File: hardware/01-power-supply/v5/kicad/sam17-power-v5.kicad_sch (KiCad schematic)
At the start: 157 parts, among them J1 KPJX-PM-4S, J10 PinHeader 1x04 P2.54mm, J2 Molex KK-254 4 pos (con llave), J5 Faston 6.3x0.8 PCB, J6 Molex KK-254 2 pos, J8 PinHeader 1x04 P2.54mm, J9 Molex KK-254 2 pos, Q2 N-MOSFET 60V 40A Ron<5mohm, SW1 Pulsador tactil 6x6mm THT, U1 Linear Tech LT1963AEST#TRPBF, U10 TI ADS1115IDGSR, U11 TI TMP1075DGKR, U12 TI INA226AIDGSR, U13 TI INA226AIDGSR, U14 TI INA226AIDGSR, U15 TI LM74502DDFR, U16 TI TPS26630PWPR, U17 TI MSP430FR2111IPW16, U18 TI TPS70933DBVR, U19 TI TPS26630PWPR, U2 Linear Tech LT3015EQ#TRPBF, U20 TI LM393BDR, U21 TI TL431BIDBZR, U22 TI TL431BIDBZR, U23 TI TL431BIDBZR, U24 TI TL431BIDBZR, U25 TI TL431BIDBZR, U4 Linear Tech LT3045EDD#TRPBF, U5 Linear Tech LT3045EDD#TRPBF, U6 Linear Tech LT3094EDD#PBF, U7 Linear Tech LT3094EDD#PBF, U8 TI INA226AIDGSR, U9 TI ISO1541D

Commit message: hardware: fuente v5, rehace el esquematico contra las hojas de datos
El esquematico anterior no habria funcionado aunque la placa estuviera
ruteada. Lo verificado contra las hojas del repo:

- Simbolos propios con el pinout inventado: TPS26630 (SHDN e IN_SYS a
  masa, IN/OUT/PowerPAD al aire), LM74502 (GND en +24 V, GATE en GND),
  MSP430 (DVCC/DVSS en dos GPIO), TRACO THN y Mornsun URB con las
  salidas cambiadas, LT3015 con el TAB (= IN) a GND, LT1963A en un
  SOT-223 que solo existe en version fija, Q2 sin ningun pad.
- Cableado: PGFB de los LT3045/LT3094 a GND y VIOC a GND, R_SET de
  120k con dos reguladores en paralelo (24 V en vez de 12 V), INA226
  U13/U14 en 0x48/0x49 chocando con ADS1115/TMP1075, BAT54S pegando las
  entradas del ADC a 0.3 V, TL431 de los crowbar cortocircuitando la
  puerta en vez de dispararla, VCAP del LM74502 al aire, EN del TPS709
  (7 V max) en +24 V, U19 colgando de un detector que mira su propia
  salida, PS3 no aislado sin camino de retorno a GND24.
- Valores: el filtro LC de la BOM no era el que analizan los
  presupuestos (con el de la BOM, U1 ve 21 V > 20 V), divisores de
  OVP/UVLO y trims de TRACO que no daban las tensiones documentadas.
- BOM: ~45 de 55 codigos LCSC eran de otra pieza.

Ahora:
- build_simbolos.py y build_huellas.py generan los simbolos y huellas
  propios desde tablas con su pagina de hoja; donde KiCad trae el
  simbolo correcto (TPS26631PWP, LT1963AEQ, LT3015Q, TL431DBZ...) se usa
  el suyo. TPS26630PWPR no existe: va el TPS26631PWPR.
- build_schematic.py escribe la hoja sin MCP (symlib + schcheck, como
  VCO y bus board), exige declarar cada patilla y cruza patillas con
  pads; ERC 0 infracciones con todas las severidades. UUID
  deterministas.
- Decisiones: GND24-GNDA unidas solo en NT1 (PS3), el LC sigue al
  analisis (22 uH / 47 uF / 0.68 ohm + 220 uF), crowbar TL431 -> PNP ->
  SCR, D-F4 referido a VREF con histeresis, D1 bidireccional, conector
  de panel fuera de la PCB (bom-chasis.csv), dos salidas 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
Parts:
- removed C3, C4: 22uF 25V X7R 1210, Capacitor_SMD:C_1210_3225Metric, symbol Device:C
- removed D10: Bourns SMBJ16A TVS, Diode_SMD:D_SMB, symbol Device:D_TVS
- removed J1: KPJX-PM-4S, sam17:Kycon_KPJX-PM-4S, symbol sam17:KPJX-PM-4S
- removed PS1: TRACO THN 30-2422WI, sam17:Converter_DCDC_TRACO_THN-30WI_THT, symbol sam17:TRACO_THN_30-2422WI
- removed PS2: Mornsun URB2405YMD-20WR3, sam17:Converter_DCDC_Mornsun_URB-YMD-20WR3_THT, symbol sam17:Mornsun_URB2405YMD-20WR3
- removed PS3: Mornsun K7805T-1000R3, sam17:Converter_DCDC_Mornsun_K78_T1000R3_SMD, symbol sam17:Mornsun_K7805T-1000R3
- removed PS4, PS5: TRACO THN 20-2413WI, sam17:Converter_DCDC_TRACO_THN-20WI_THT, symbol sam17:TRACO_THN_20-2413WI
- removed Q2: N-MOSFET 60V 40A Ron<5mohm, Package_TO_SOT_SMD:TDSON-8-1, symbol Device:Q_NMOS
- removed R19, R29, R30: 20 mohm 1% 1W 2512, Resistor_SMD:R_2512_6332Metric, symbol Device:R_Shunt
- removed R20: 100 mohm 1% 1W 2512, Resistor_SMD:R_2512_6332Metric, symbol Device:R_Shunt
- removed U1: Linear Tech LT1963AEST#TRPBF, Package_TO_SOT_SMD:SOT-223-3_TabPin2, symbol sam17:LT1963AEST
- removed U15: TI LM74502DDFR, Package_TO_SOT_SMD:SOT-23-8, symbol sam17:LM74502DDFR
- removed U16, U19: TI TPS26630PWPR, Package_SO:HTSSOP-20-1EP_4.4x6.5mm_P0.65mm_EP3.4x6.5mm, symbol sam17:TPS26630PWPR
- removed U18: TI TPS70933DBVR, Package_TO_SOT_SMD:SOT-23-5, symbol Regulator_Linear:LP2985-3.3
- removed U2: Linear Tech LT3015EQ#TRPBF, Package_TO_SOT_SMD:TO-263-5_TabPin3, symbol sam17:LT3015EQ
- removed U20: TI LM393BDR, Package_SO:SOIC-8_3.9x4.9mm_P1.27mm, symbol sam17:LM393BDR
- removed U21, U22, U23, U24, U25: TI TL431BIDBZR, Package_TO_SOT_SMD:SOT-23, symbol Reference_Voltage:TL431LP
- added C10, C30, C31, C32, C33, C34, C35, C9: 100nF 50V X7R, Capacitor_SMD:C_0805_2012Metric, symbol Device:C
- added C11, C13: 22nF 50V X7R, Capacitor_SMD:C_0805_2012Metric, symbol Device:C
- added C12: 1nF 50V C0G, Capacitor_SMD:C_0805_2012Metric, symbol Device:C
- added C14: 100uF 50V, Capacitor_SMD:CP_Elec_8x10, symbol Device:C_Polarized
- added C15: 10uF 50V X7R, Capacitor_SMD:C_1210_3225Metric, symbol Device:C
- added C16, C36, C37, C38: 22uF 25V X7R, Capacitor_SMD:C_1210_3225Metric, symbol Device:C
- added C29: 100uF 25V, Capacitor_SMD:CP_Elec_6.3x7.7, symbol Device:C_Polarized
- added C3, C4: 47uF 35V, Capacitor_SMD:CP_Elec_6.3x7.7, symbol Device:C_Polarized
- added D10: SMBJ16A, Diode_SMD:D_SMB, symbol Device:D_Zener
- added D2: BZT52C30, Diode_SMD:D_SOD-123, symbol Device:D_Zener
- added J1: Bornera 2P 5.0 mm, TerminalBlock:TerminalBlock_MaiXu_MX126-5.0-02P_1x02_P5.00mm, symbol Connector:Conn_01x02_Pin
- added J3: Bornera 4P 5.08 mm, TerminalBlock_Phoenix:TerminalBlock_Phoenix_MKDS-1,5-4-5.08_1x04_P5.08mm_Horizontal, symbol Connector:Conn_01x04_Pin
- added J7: Molex KK-254 4P, Connector_Molex:Molex_KK-254_AE-6410-04A_1x04_P2.54mm_Vertical, symbol Connector:Conn_01x04_Pin
- added NT1: NetTie GND24-GNDA, NetTie:NetTie-2_SMD_Pad2.0mm, symbol Device:NetTie_2
- added PS1: THN 30-2422WI, Converter_DCDC:Converter_DCDC_TRACO_THL30-xxxxWI_THT, symbol sam17:TRACO_THN_Dual
- added PS2: URB2405YMD-20WR3, sam17:Converter_DCDC_Mornsun_URB_YMD-20WR3_Horizontal_THT, symbol sam17:Mornsun_URB_YMD-20WR3
- added PS3: K7805T-1000R3, sam17:Converter_DCDC_Mornsun_K78_T-1000R3_SMD, symbol sam17:Mornsun_K78xxT-1000R3
- added PS4, PS5: THN 20-2413WI, Converter_DCDC:Converter_DCDC_TRACO_THL30-xxxxWI_THT, symbol sam17:TRACO_THN_Single
- added Q2: CSD18534Q5A, Package_TO_SOT_SMD:TDSON-8-1, symbol Transistor_FET:CSD18534Q5A
- added Q3, Q4, Q5, Q6: MMBT3906, Package_TO_SOT_SMD:SOT-23, symbol Transistor_BJT:MMBT3906
- added R19, R29, R30: 0.02, Resistor_SMD:R_2512_6332Metric, symbol Device:R
- added R20: 0.1, Resistor_SMD:R_2512_6332Metric, symbol Device:R
- added R61, R62: 120k 0.1%, Resistor_SMD:R_0805_2012Metric, symbol Device:R
- added R63: 1.2k, Resistor_SMD:R_0805_2012Metric, symbol Device:R
- added R64: 220, Resistor_SMD:R_0805_2012Metric, symbol Device:R
- added R65: 47k, Resistor_SMD:R_0805_2012Metric, symbol Device:R
- added R66, R68, R74, R75, R76, R77: 10k, Resistor_SMD:R_0805_2012Metric, symbol Device:R
- added R67: 6.8M, Resistor_SMD:R_0805_2012Metric, symbol Device:R
- added R69: 10M, Resistor_SMD:R_0805_2012Metric, symbol Device:R
- added R70, R71, R72, R73: 1k, Resistor_SMD:R_0805_2012Metric, symbol Device:R
- added R78, R79, R80, R81: 100, Resistor_SMD:R_0805_2012Metric, symbol Device:R
- added U1: LT1963AEQ, Package_TO_SOT_SMD:TO-263-5_TabPin3, symbol Regulator_Linear:LT1963AEQ
- added U15: LM74502DDFR, Package_TO_SOT_SMD:SOT-23-8, symbol sam17:LM74502DDF
- added U16, U19: TPS26631PWPR, Package_SO:HTSSOP-20-1EP_4.4x6.5mm_P0.65mm_EP3.4x6.5mm_Mask2.96x2.96mm_ThermalVias, symbol Power_Management:TPS26631PWP
- added U18: TPS70933DBVR, Package_TO_SOT_SMD:SOT-23-5, symbol sam17:TPS70933DBV
- added U2: LT3015EQ, Package_TO_SOT_SMD:TO-263-5_TabPin3, symbol Regulator_Linear:LT3015Q
- added U20: LM393B, Package_SO:SOIC-8_3.9x4.9mm_P1.27mm, symbol Comparator:LM393
- added U21, U22, U23, U24, U25: TL431BI, Package_TO_SOT_SMD:SOT-23, symbol Reference_Voltage:TL431DBZ
- C1, C2: value 47uF 25V electrolitico SMD -> 220uF 35V; footprint Capacitor_SMD:CP_Elec_6.3x7.7 -> Capacitor_SMD:CP_Elec_8x10; LCSC (none) -> C178562; MPN (none) -> EEEFK1V221P
- C17, C18: value 10uF 25V X7R 1206 -> 47uF 35V; footprint Capacitor_SMD:C_1206_3216Metric -> Capacitor_SMD:CP_Elec_6.3x7.7; LCSC (none) -> C249923; MPN (none) -> VZH470M1VTR-0607
- C19, C21: value 470nF 25V X7R 0805 -> 470nF 50V X7R; LCSC (none) -> C13967; MPN (none) -> CL21B474KBFNNNE
- C20, C22: value 10uF 25V X7R 1206 -> 22uF 25V X7R; footprint Capacitor_SMD:C_1206_3216Metric -> Capacitor_SMD:C_1210_3225Metric; LCSC (none) -> C21397; MPN (none) -> GRM32ER71E226KE15L
- C23, C24, C25, C26, C27, C28, C5, C6: value 100nF 50V X7R 0805 -> 100nF 50V X7R; LCSC (none) -> C49678; MPN (none) -> CC0805KRX7R9BB104
- C7: value 1uF 50V X7R 0805 -> 1uF 50V X7R; LCSC (none) -> C28323; MPN (none) -> CL21B105KBFNNNE
- C8: value 1uF 50V X7R 0805 -> 4.7uF 25V X7R; LCSC (none) -> C354262; MPN (none) -> CC0805KKX7R8BB475
- D1: value Bourns SMBJ26A TVS -> SMBJ26CA; LCSC (none) -> C83332; MPN (none) -> SMBJ26CA
- D11: value Schottky BAT54WS 30V 200mA -> BAT54WS; LCSC (none) -> C124205; MPN (none) -> BAT54WS-7-F
- D12, D13: value 1N4001 / S1M -> S1M; LCSC (none) -> C144860; MPN (none) -> S1M-E3/61T
- D14, D15, D16, D17: value Diodo Schottky doble BAT54S -> BAT54S; LCSC (none) -> C19726; MPN (none) -> BAT54SLT1G
- D18: value LED azul 0805 -> LED verde 0805; LCSC (none) -> C98221; MPN (none) -> LTST-C170KGKT
- D3: LCSC (none) -> C99771; MPN (none) -> 204-10SURD/S530-A3-L
- D4: LCSC (none) -> C85160; MPN (none) -> 204-10UYD/S530-A3-L
- D6: LCSC (none) -> C181864; MPN (none) -> 204-10SYGD/S530-E2-L
- D7: LCSC (none) -> C86881; MPN (none) -> 204-10SUBC/S400-A4
- F2, F3: value Bourns SF-1206F300-2 3.0A Fast Blow -> SF-1206F300-2 3A; LCSC (none) -> C208499; MPN (none) -> SF-1206F300-2
- F4: value Bourns SF-1206F200-2 2.0A Fast Blow -> SF-1206F200-2 2A; LCSC (none) -> C719183; MPN (none) -> SF-1206F200-2
- F5: value Bourns SF-1206F400-2 4.0A Fast Blow -> 0466004 4A; LCSC (none) -> C187596; MPN (none) -> 0466004.NRHF
- FB1, FB2: value Ferrita 60 ohm @ 100MHz 2A -> BLM21PG600SN1D; footprint Resistor_SMD:R_0805_2012Metric -> Inductor_SMD:L_0805_2012Metric; LCSC (none) -> C18305; MPN (none) -> BLM21PG600SN1D
- J10, J8: value PinHeader 1x04 P2.54mm -> PinHeader 1x04; LCSC (none) -> C2691448; MPN (none) -> PZ254V-11-04P
- J2: value Molex KK-254 4 pos (con llave) -> Molex KK-254 4P; LCSC (none) -> C504991; MPN (none) -> 22-27-2041
- J5: MPN (none) -> 3866A.68
- J6, J9: value Molex KK-254 2 pos -> Molex KK-254 2P; LCSC (none) -> C293316; MPN (none) -> 22-27-2021
- L2, L3: value 10uH 2.5A DCR<35mohm -> 22uH SRR1260-220M; LCSC (none) -> C3224283; MPN (none) -> SRR1260-220M
- R1, R2: value 2.2k 1/4W 0805 -> 2.2k; LCSC (none) -> C17520; MPN (none) -> 0805W8F2201T5E
- R10, R9: value 120k 0.1% 25ppm 0805 -> 120k 0.1%; LCSC (none) -> C865161; MPN (none) -> RT0805BRD07120KL
- R11: value 4.02k 1% 0805 -> 4.02k; LCSC (none) -> C17663; MPN (none) -> 0805W8F4021T5E
- R12, R35: value 49.9k 0.1% 0805 -> 49.9k 0.1%; LCSC (none) -> C469661; MPN (none) -> RT0805BRD0749K9L
- R13: value 3.32k 0.1% 0805 -> 1.62k 0.1%; LCSC (none) -> C50670348; MPN (none) -> TC0525B1621T5G
- R14: value 2.00k 0.1% 0805 -> 1.96k 0.1%; LCSC (none) -> C2093012; MPN (none) -> TNPW08051K96BEEN
- R15, R16, R17, R18: value 20 mohm 1% 1W 2512 -> 0.02; LCSC (none) -> C553969; MPN (none) -> WSL2512R0200FEA
- R21, R22, R23, R24: value 100k 0.1% 0805 -> 100k 0.1%; LCSC (none) -> C122537; MPN (none) -> RT0805BRD07100KL
- R25, R26, R27, R28: value 20.0k 0.1% 0805 -> 20.0k 0.1%; LCSC (none) -> C469660; MPN (none) -> RT0805BRD0720KL
- R3, R4: value 680R 1/4W 0805 -> 680; LCSC (none) -> C17798; MPN (none) -> 0805W8F6800T5E
- R31: value 1.0k 1% 0805 -> 220; LCSC (none) -> C17557; MPN (none) -> 0805W8F2200T5E
- R32, R33: value 240k 1% 0805 -> 45.3k; LCSC (none) -> C17701; MPN (none) -> 0805W8F4532T5E
- R34: value 18.2k 1% 0805 -> 18.2k; LCSC (none) -> C17497; MPN (none) -> 0805W8F1822T5E
- R36: value 3.83k 0.1% 0805 -> 3.9k 0.1%; LCSC (none) -> C865471; MPN (none) -> RT0805BRD073K9L
- R37, R38: value 0.5 ohm 1% 1206 -> 0.68; LCSC (none) -> C19108; MPN (none) -> 1206W4F680LT5E
- R39: value 49.9k 0.1% 0805 -> 47.5k 0.1%; LCSC (none) -> C865514; MPN (none) -> RT0805BRD0747K5L
- R40, R47, R48, R50, R52: value 10.0k 0.1% 0805 -> 10.0k 0.1%; LCSC (none) -> C110775; MPN (none) -> RT0805BRD0710KL
- R41: value 49.9k 0.1% 0805 -> 10.2k 0.1%; LCSC (none) -> C865134; MPN (none) -> RT0805BRD0710K2L
- R42: value 10.0k 0.1% 0805 -> 59.0k 0.1%; LCSC (none) -> C865570; MPN (none) -> RT0805BRD0759KL
- R43: value 100k 1% 0805 -> 100k; LCSC (none) -> C149504; MPN (none) -> 0805W8F1003T5E
- R44: value 10.0k 1% 0805 -> 10k; LCSC (none) -> C17414; MPN (none) -> 0805W8F1002T5E
- R45, R46: value 45.3k 0.1% 0805 -> 45.3k 0.1%; LCSC (none) -> C866072; MPN (none) -> RT0805BRE0745K3L
- R49: value 13.3k 0.1% 0805 -> 13.3k 0.1%; LCSC (none) -> C865182; MPN (none) -> RT0805BRD0713K3L
- R5: value 8.66k 0.1% 0805 -> 9.31k 0.1%; LCSC (none) -> C865720; MPN (none) -> RT0805BRD079K31L
- R51: value 12.7k 0.1% 0805 -> 12.7k 0.1%; LCSC (none) -> C50670219; MPN (none) -> TC0525B1272T5G
- R53, R54, R55, R56: value 1.0k 1% 0805 -> 1k; LCSC (none) -> C17513; MPN (none) -> 0805W8F1001T5E
- R57, R58, R59, R60: value 2.2k 1% 0805 -> 2.2k; LCSC (none) -> C17520; MPN (none) -> 0805W8F2201T5E
- R6, R8: value 1.00k 0.1% 0805 -> 1.00k 0.1%; LCSC (none) -> C110774; MPN (none) -> RT0805BRD071KL
- R7: value 9.09k 0.1% 0805 -> 9.09k 0.1%; LCSC (none) -> C865717; MPN (none) -> RT0805BRD079K09L
- RV2, RV3: value Bourns 3296W-1-102 (1k trimmer) -> 1k 3296W; LCSC (none) -> C57089; MPN (none) -> 3296W-1-102LF
- SCR1, SCR2, SCR3, SCR4: value NXP BT151-500R Tiristor TO-220 -> BT151-500R; LCSC (none) -> C9211; MPN (none) -> BT151-500R,127
- SW1: value Pulsador tactil 6x6mm THT -> Pulsador 6x6; LCSC (none) -> C93157; MPN (none) -> B3F-1000
- TP1, TP10, TP11, TP2, TP3, TP4, TP5, TP6, TP7, TP8, TP9: value TestPoint Pad D2.0mm -> TestPoint; MPN (none) -> —
- U10: value TI ADS1115IDGSR -> ADS1115IDGS; footprint Package_SO:MSOP-10_3x3mm_P0.5mm -> Package_SO:TSSOP-10_3x3mm_P0.5mm; LCSC (none) -> C37593; MPN (none) -> ADS1115IDGSR
- U11: value TI TMP1075DGKR -> TMP1075DGK; LCSC (none) -> C2864807; MPN (none) -> TMP1075DGKR
- U12, U13, U14, U8: value TI INA226AIDGSR -> INA226; footprint Package_SO:MSOP-10_3x3mm_P0.5mm -> Package_SO:TSSOP-10_3x3mm_P0.5mm; LCSC (none) -> C49851; MPN (none) -> INA226AIDGSR
- U17: value TI MSP430FR2111IPW16 -> MSP430FR2111IPW16; LCSC (none) -> C2052845; MPN (none) -> MSP430FR2111IPW16R
- U4, U5: value Linear Tech LT3045EDD#TRPBF -> LT3045EDD; footprint Package_DFN_QFN:DFN-10-1EP_3x3mm_P0.5mm_EP1.65x2.38mm -> Package_DFN_QFN:DFN-10-1EP_3x3mm_P0.5mm_EP1.65x2.38mm_ThermalVias; LCSC (none) -> C514420; MPN (none) -> LT3045EDD#TRPBF
- U6, U7: value Linear Tech LT3094EDD#PBF -> LT3094EDD; footprint Package_DFN_QFN:DFN-12-1EP_3x3mm_P0.45mm_EP1.65x2.38mm -> Package_DFN_QFN:DFN-12-1EP_3x3mm_P0.45mm_EP1.65x2.38mm_ThermalVias; LCSC (none) -> C670493; MPN (none) -> LT3094EDD#TRPBF
- U9: value TI ISO1541D -> ISO1541; LCSC (none) -> C143028; MPN (none) -> ISO1541DR
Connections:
- net +12V_FUSED_RACK: now also R29.1; no longer R45.1, SCR1.2 (A), U13.8 (Vbus), U13.9 (Vin-)
- net +12V_RAW_RACK: now also PS1.3 (+Vout)
- net +12V_ULTRA: now also J7.4 (Pin_4), R19.2
- net +13V1: now also U4.6 (PGFB), U5.6 (PGFB), C36.1, U1.4 (OUT)
- net +15V5_EFUSE: now also U19.18 (OUT), U19.19 (OUT), U19.20 (OUT)
- net +15V5_FILT: now also D10.1 (K), U1.2 (IN)
- net +15V5_LC: now also C3.1; no longer C24.1, C25.1, C26.1, C27.1, D14.2 (K), D15.2 (K), D16.2 (K), D17.2 (K), F4.1, R25.2, R27.2, R28.2, R41.1, R44.1, R57.1, R58.1, U10.8 (VDD), U11.7 (A0), U11.8 (V+), U12.10 (Vin+), U12.2 (A0), U12.6 (VS), U12.8 (Vbus), U12.9 (Vin-), U13.6 (VS), U14.2 (A0), U14.6 (VS), U8.6 (VS), U9.1 (VCC1)
- net +15V5_RAW: now also PS4.3 (+Vout), U19.1 (IN), U19.2 (IN), U19.3 (IN), U19.6 (IN_SYS); no longer R32.2
- net +24V_PROT: now also Q2.5 (D), R64.1, U16.1 (IN), U16.2 (IN), U16.3 (IN), U16.6 (IN_SYS); no longer C7.1
- net +24V_RAW: now also C10.1, C9.2, J1.1 (Pin_1), Q2.1 (S), Q2.2 (S), Q2.3 (S), U15.1 (EN/UVLO), U15.5 (VS), U15.8 (SRC)
- net +24V_SW: now also C14.1, C15.1, PS1.1 (+Vin), PS2.3 (Vin), PS3.1 (+Vin), PS3.2 (+Vin), PS4.1 (+Vin), PS5.1 (+Vin), U16.18 (OUT), U16.19 (OUT), U16.20 (OUT)
- net +3V3_MCU: now also U17.5 (DVCC), R65.1, R66.1, U18.5 (OUT); no longer U17.13 (VDD)
- net +5V_DIG: now also Q6.2 (E), R77.1
- net +5V_FUSED_RACK: now also R30.1; no longer J6.1 (Pin_1), R3.1, R49.1, SCR3.2 (A), TP5.1, U14.8 (Vbus), U14.9 (Vin-)
- net +5V_RAW_DIG: now also C29.1, PS2.4 (+Vo)
- net -12V9: now also U6.5 (PGFB), U7.5 (PGFB), C37.2, U2.5 (OUT)
- net -12V_RACK: now also J3.3 (Pin_3), U23.3 (A)
- net -12V_RAW_RACK: now also PS1.5 (-Vout)
- net -12V_ULTRA: now also J7.1 (Pin_1)
- net -15V5_FILT: now also U2.3 (IN)
- net -15V5_LC: now also C4.2
- net -15V5_RAW: now also PS5.5 (-Vout)
- net ADJ_U1: now also U1.5 (ADJ)
- net ADJ_U2: now also U2.4 (ADJ)
- net AIN0: now also D14.3 (COM); no longer D14.1 (A)
- net AIN1: now also D15.3 (COM); no longer D15.1 (A)
- net AIN2: now also D16.3 (COM); no longer D16.1 (A)
- net AIN3: now also D17.3 (COM); no longer D17.1 (A)
- net FLT_M5: now also U17.1 (P1.1), R66.2, U16.15 (~{FLT}); no longer U17.2 (P1.1_FLT)
- net GATE_Q2: now also Q2.4 (G), U15.6 (GATE)
- net GATE_SCR1: now also R78.2
- net GATE_SCR2: now also R79.2
- net GATE_SCR3: now also R80.2
- net GATE_SCR4: now also R81.2
- net GND24: now also U17.6 (DVSS), C10.2, C11.2, C12.2, C14.2, C15.2, C16.2, D2.2 (A), J1.2 (Pin_2), NT1.1, PS1.2 (-Vin), PS2.2 (GND), PS3.3 (GND), PS3.7 (GND), PS4.2 (-Vin), PS5.2 (-Vin), U15.2 (GND), U15.7 (OV), U16.16 (PGTH), U16.21 (GND), U16.9 (GND), U18.2 (GND); no longer U17.14 (VSS)
- net GNDA: now also D14.1 (A), D15.1 (A), D16.1 (A), D17.1 (A), R32.2, C13.2, C3.2, C30.2, C31.2, C32.2, C33.2, C34.2, C35.2, C36.2, C37.1, C38.2, C4.1, D10.2 (A), J3.2 (Pin_2), J7.2 (Pin_2), J7.3 (Pin_3), NT1.2, PS1.4 (Common), PS4.5 (-Vout), PS5.3 (+Vout), Q4.2 (E), R61.2, R62.2, R68.2, R75.1, U1.3 (GND), U19.12 (MODE), U19.16 (PGTH), U19.21 (GND), U19.7 (UVLO), U19.9 (GND), U2.2 (GND), U20.4 (V-), U21.3 (A), U22.3 (A), U24.3 (A); no longer D14.3 (COM), D15.3 (COM), D16.3 (COM), D17.3 (COM), U4.6 (PGFB), U5.6 (PGFB), U6.5 (PGFB), U6.7 (VIOC), U7.5 (PGFB), U7.7 (VIOC)
- net GNDD: now also C29.2, PS2.6 (0V), U25.3 (A)
- net ILIM_U16: now also U16.11 (ILIM)
- net ILIM_U19: now also U19.11 (ILIM)
- net LED_CTRL: now also U17.14 (P1.4); no longer U17.5 (P1.4_LED)
- net MCU_RST: now also U17.4 (RST/NMI/SBWTDIO), C12.1, R65.2; no longer U17.11 (RST)
- net MCU_TEST: now also U17.3 (TEST/SBWTCK); no longer U17.12 (TEST)
- net OUTS_POS: now also C38.1, R19.1
- net REF_CB1: now also U22.2 (REF)
- net REF_CB2: now also U23.2 (REF)
- net REF_CB3: now also U24.2 (REF)
- net REF_CB4: now also U25.2 (REF)
- net SDA_A: no longer U13.1 (A1), U14.1 (A1)
- net SENSE_NEG: now also C35.1, U20.6 (-)
- net SENSE_POS: now also C34.1, R67.2, U20.3 (+)
- net SET_NEG: now also R62.1
- net SET_POS: now also R61.1
- net SHDN_CASCADE: now also R67.1, R69.1, U1.1 (~{SHDN}), U2.1 (~{SHDN}), U20.1, U20.7
- net SHDN_M5: now also U17.15 (P1.3), U16.13 (~{SHDN}); no longer U17.4 (P1.3_SHDN)
- net SW_RESET: now also U17.13 (P1.5); no longer U17.6 (P1.5_RSTBTN)
- net TRIM_PS4: now also PS4.4 (Trim)
- net TRIM_PS5: now also PS5.4 (Trim)
- net UVLO_U16: now also U16.7 (UVLO)
- net VREF_2V5: now also R41.1, R63.2, U20.2 (-), U21.1 (K), U21.2 (REF)
- net OVPR_U16 renamed OVP_U16
- net OVP_U16: now also U16.8 (OVP)
- net OVPR_U19 renamed OVP_U19
- net OVP_U19: now also U19.8 (OVP)
- new net +12V_RACK: J3.1 (Pin_1), Q3.2 (E), R29.2, R45.1, R74.1, SCR1.2 (A), U13.8 (Vbus), U13.9 (Vin-)
- new net +24V_LDO: C7.1, D2.1 (K), R64.2, U18.1 (IN)
- new net +5V_AUX: C24.1, C25.1, C26.1, C27.1, C30.1, C31.1, C32.1, C33.1, D14.2 (K), D15.2 (K), D16.2 (K), D17.2 (K), J6.1 (Pin_1), R20.2, R25.2, R27.2, R28.2, R44.1, R57.1, R58.1, R63.1, U10.8 (VDD), U11.7 (A0), U11.8 (V+), U12.2 (A0), U12.6 (VS), U12.8 (Vbus), U12.9 (Vin-), U13.1 (A1), U13.6 (VS), U14.1 (A1), U14.2 (A0), U14.6 (VS), U20.8 (V+), U8.6 (VS), U9.1 (VCC1)
- new net +5V_RACK: J3.4 (Pin_4), Q5.2 (E), R3.1, R30.2, R49.1, R76.1, SCR3.2 (A), TP5.1, U14.8 (Vbus), U14.9 (Vin-)
- new net +5V_RAW_RACK: C16.1, F4.1, PS3.4 (+Vout), PS3.5 (+Vout), R20.1, U12.10 (Vin+)
- new net DVDT_U16: C11.1, U16.10 (dVdT)
- new net DVDT_U19: C13.1, U19.10 (dVdT)
- new net QB_CB1: Q3.1 (B), R70.1, R74.2
- new net QB_CB2: Q4.1 (B), R71.1, R75.2
- new net QB_CB3: Q5.1 (B), R72.1, R76.2
- new net QB_CB4: Q6.1 (B), R73.1, R77.2
- new net QC_CB1: Q3.3 (C), R78.1
- new net QC_CB2: Q4.3 (C), R79.1
- new net QC_CB3: Q5.3 (C), R80.1
- new net QC_CB4: Q6.3 (C), R81.1
- new net REF0_NEG: R68.1, R69.2, U20.5 (+)
- new net TLK_CB1: R70.2, U22.1 (K)
- new net TLK_CB2: R71.2, U23.1 (K)
- new net TLK_CB3: R72.2, U24.1 (K)
- new net TLK_CB4: R73.2, U25.1 (K)
- new net VCAP_U15: C9.1, U15.4 (VCAP)
- no-connect marks 0 -> 41
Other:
- note added: "BLOQUE CON: Conectores"
- note added: "BLOQUE DCDC: Convertidores: THN 30 (+-12 rack), URB (+5 digital M1), K78 (+5 rack), 2 x THN 20 (+-15.5)"
- note added: "BLOQUE DF4: Detector D-F4: LM393 + TL431, umbral 14.5 V con histeresis"
- note added: "BLOQUE DF6: Rack: fusibles y crowbars D-F6 (TL431 -> PNP -> BT151)"
- note added: "BLOQUE LC: Tope M3 (#334): TPS26631 + filtro LC 22 uH / 47 uF / 0.68 ohm + 220 uF + SMBJ16A"
- note added: "BLOQUE M5: Entrada 24 V, polaridad (LM74502 + CSD18534Q5A), eFuse U16 y supervisor M5"
- note added: "BLOQUE PRE: Pre-reguladores LT1963A (+13.1 V) y LT3015 (-12.9 V)"
- note added: "BLOQUE TEL: Telemetria I2C: 4 x INA226, ADS1115, TMP1075 e ISO1541"
- note added: "BLOQUE ULTRA: Cascada ultra: 2 x LT3045 y 2 x LT3094 en paralelo, R_SET = 60k"
- note added: "PWR_FLAG: redes que alimenta algo pasivo o un conector"
- note removed: "BLOQUE 1: Entrada 24V, Supervisor M5 (MSP430FR2111 + TPS26630) y Proteccion Inversa (LM74502)"
- note removed: "BLOQUE 2: DC-DCs (TRACO THN 30WI +-12V, Mornsun URB 5V DIG, Mornsun K78 5V RACK, 2x THN 20WI +-15.5V)"
- note removed: "BLOQUE 3: Filtro LC y eFuse TPS26630 M3 / #334 + Bourns SMBJ16A"
- note removed: "BLOQUE 4: Secuenciador D-F4 / M4 (LM393B + TL431BI)"
- note removed: "BLOQUE 5: Cascada Primera Etapa (LT1963A + LT3015)"
- note removed: "BLOQUE 6: Cascada Segunda Etapa Ultra-Bajo Ruido (2x LT3045 + 2x LT3094)"
- note removed: "BLOQUE 7: Protecciones Rack Crowbar D-F6 (4x BT151-500R + TL431BI + Fuses)"
- note removed: "BLOQUE 8: Telemetria I2C Aislada (4x INA226, ADS1115, TMP1075, ISO1541)"
- note removed: "SAM17 FUENTE v5 (LADRILLO EXTERNO 24V + 5 CONVERTIDORES DC-DC)"
- company: SAM17 — Sintetizador analogico modular -> SAM17 - Sintetizador analogico modular
- title: SAM17 Modulo 01 v5 — Fuente de Alimentacion Ladrillo 24V y DC-DCs -> SAM17 Modulo 01 v5 - Fuente: ladrillo 24 V y convertidores DC-DC

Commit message: hardware: fuente v5, SHDN de U16 con pull-down, FLT de U19 al MSP430 y U19 con rueda libre
- U16: R83 (47k) de SHDN a GND24. El pin tiene pull-up interno (2,48 a
  3,3 V en vacio, hasta 10 uA, tps2663.pdf p. 7): sin pull-down, U16
  encendia en cada enchufe, reset o sesion de programacion antes de que
  el MCU leyera la bandera de abandono de la FRAM.
- U19: FLT a P1.2 del MSP430, con pull-up R84. No va al SHDN de U16: el
  TPS26631 baja FLT mientras su entrada esta en UVLO (p. 19) y U16 no
  arrancaria nunca.
- U19: UVLO a IN_SYS por R82 (6,8M, p. 20). A GND elegia el umbral
  interno de 15,1 a 15,9 V (p. 6), por encima del riel de 15,5 V.
- D19 (SS34) de OUT de U19 a GNDA: al abrir U19 la corriente de L2 no
  tenia camino y llevaba OUT por debajo de sus -0,3 V (p. 5, 36 y 38).
- U18: R64 pasa a 1k y D2 a BZT52C24. Con el BZT52C30 el TPS709 llegaba a
  32 V con 2 mA; ahora no pasa de 26,4 V con D1 en 42,1 V.
- R53 a R56 (R_GK) pasan a 100 ohm: el dV/dt de 200 V/us del BT151 se da
  con R_GK = 100 ohm (nxp-bt151-500r.pdf p. 6).

check_netlist comprueba cada uno; con la netlist anterior salen los nueve
en rojo.
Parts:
- added D19: SS34, Diode_SMD:D_SMA, symbol Device:D_Schottky
- added R82: 6.8M, Resistor_SMD:R_0805_2012Metric, symbol Device:R
- added R83: 47k, Resistor_SMD:R_0805_2012Metric, symbol Device:R
- added R84: 10k, Resistor_SMD:R_0805_2012Metric, symbol Device:R
- D2: value BZT52C30 -> BZT52C24; LCSC C163721 -> C171749; MPN BZT52C30-7-F -> BZT52C24-7-F
- R53, R54, R55, R56: value 1k -> 100; LCSC C17513 -> C17408; MPN 0805W8F1001T5E -> 0805W8F1000T5E
- R64: value 220 -> 1k; LCSC C17557 -> C17513; MPN 0805W8F2200T5E -> 0805W8F1001T5E
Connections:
- net +15V5_EFUSE: now also D19.1 (K)
- net +15V5_RAW: now also R82.1
- net +3V3_MCU: now also R84.1
- net GND24: now also R83.2
- net GNDA: now also D19.2 (A); no longer U19.7 (UVLO)
- net SHDN_M5: now also R83.1
- net FLT_U19: now reaches U19.15 (~{FLT})
- net FLT_U19: now also U17.16 (P1.2), R84.2
- new net UVLO_U19: R82.2, U19.7 (UVLO)
- no-connect marks 41 -> 39
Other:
- moved on the sheet: C1, C11, C12, C13, C14, C15, C16, C17, C18, C19, C2, C20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

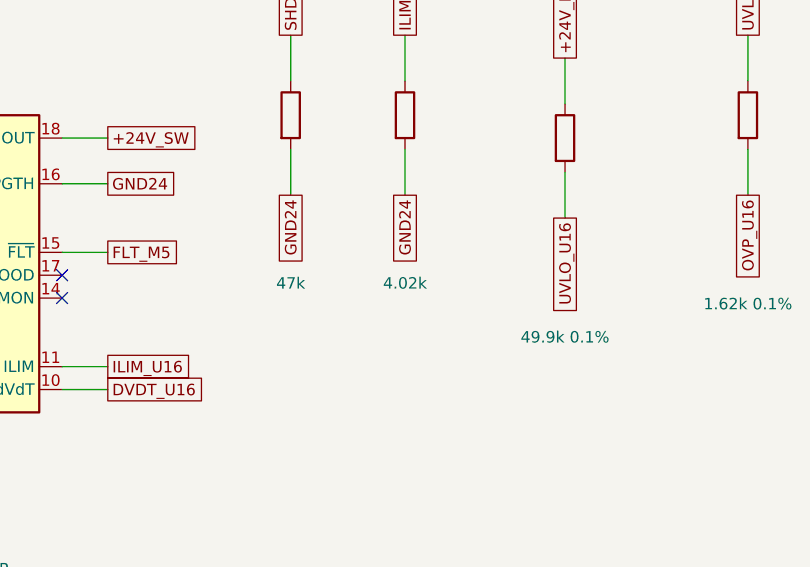
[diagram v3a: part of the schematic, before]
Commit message: hardware: fuente v5, placa y fabricacion con R11 de 3,74 kOhm
build_pcb.py --desde-ruteo copia ahora tambien el valor de cada huella
desde el netlist, asi que un cambio de valor no pide otro Freerouting. La
placa sale del ruteo guardado de la corrida anterior:

- El cobre es el mismo salvo una conexion del rescate en +24V_RAW hasta
  U15.1, que pasa de 5 tramos a 2 (1506 pistas, 285 vias).
- DRC (kicad-cli 10.0.3, todas las severidades, zonas rellenas y paridad
  con el esquematico): 0 infracciones, 0 sin conectar, 0 de paridad.

lcsc_snapshot.csv entra C2960937 y sale C17663. Esquematico, netlist, fab/
y pcb/ regenerados.
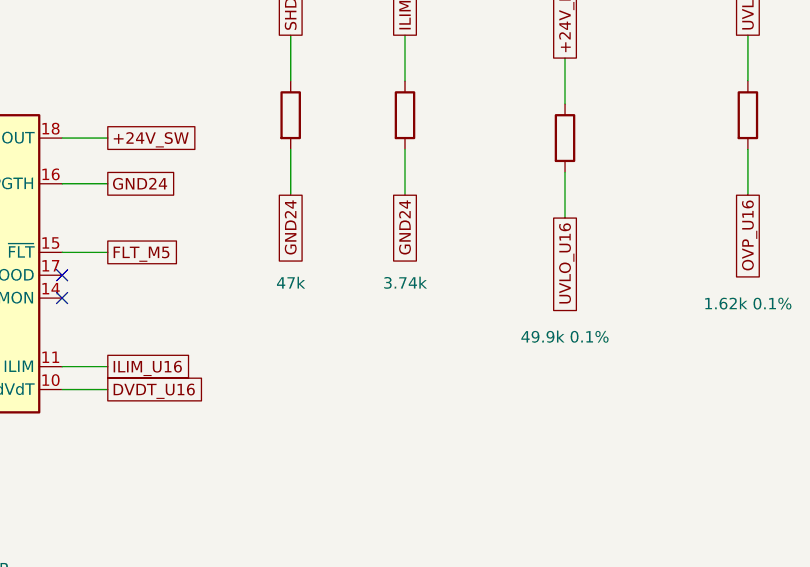
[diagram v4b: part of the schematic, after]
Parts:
- R11: value 4.02k -> 3.74k; LCSC C17663 -> C2960937; MPN 0805W8F4021T5E -> FRC0805F3741TS
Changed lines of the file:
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@@
 			)
 		)
-		(property "Value" "4.02k"
+		(property "Value" "3.74k"
 			(at 106.68 132.98 0)
 			(show_name no)
@@
 			)
 		)
-		(property "LCSC" "C17663"
+		(property "LCSC" "C2960937"
 			(at 106.68 114.3 0)
 			(hide yes)
@@
 			)
 		)
-		(property "MPN" "0805W8F4021T5E"
+		(property "MPN" "FRC0805F3741TS"
 			(at 106.68 114.3 0)
 			(hide yes)

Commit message: hardware: fuente v5, placa y fabricacion con R11 de vuelta en 4,02 kOhm
Desde el ruteo guardado, con build_pcb.py --desde-ruteo: el cobre es el de
la placa anterior, tramo a tramo (1506 pistas, 285 vias). DRC (kicad-cli
10.0.3, todas las severidades, zonas rellenas y paridad con el
esquematico): 0 infracciones, 0 sin conectar, 0 de paridad.

lcsc_snapshot.csv vuelve a C17663 y sale C2960937.
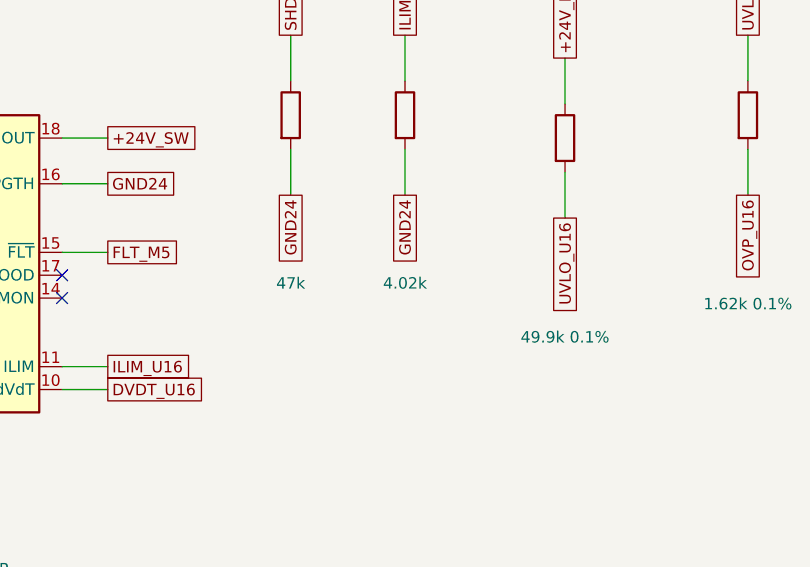
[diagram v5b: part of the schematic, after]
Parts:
- R11: value 3.74k -> 4.02k; LCSC C2960937 -> C17663; MPN FRC0805F3741TS -> 0805W8F4021T5E
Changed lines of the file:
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@@
 			)
 		)
-		(property "Value" "3.74k"
+		(property "Value" "4.02k"
 			(at 106.68 132.98 0)
 			(show_name no)
@@
 			)
 		)
-		(property "LCSC" "C2960937"
+		(property "LCSC" "C17663"
 			(at 106.68 114.3 0)
 			(hide yes)
@@
 			)
 		)
-		(property "MPN" "FRC0805F3741TS"
+		(property "MPN" "0805W8F4021T5E"
 			(at 106.68 114.3 0)
 			(hide yes)
